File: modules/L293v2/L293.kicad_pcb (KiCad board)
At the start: 2 copper layers, 40.6 x 40.6 mm, 44 parts, among them J1 2, J10 11, J11 12, J12 13, J13 A0, J14 A1, J15 A2, J16 A3, J17 A4, J18 A5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

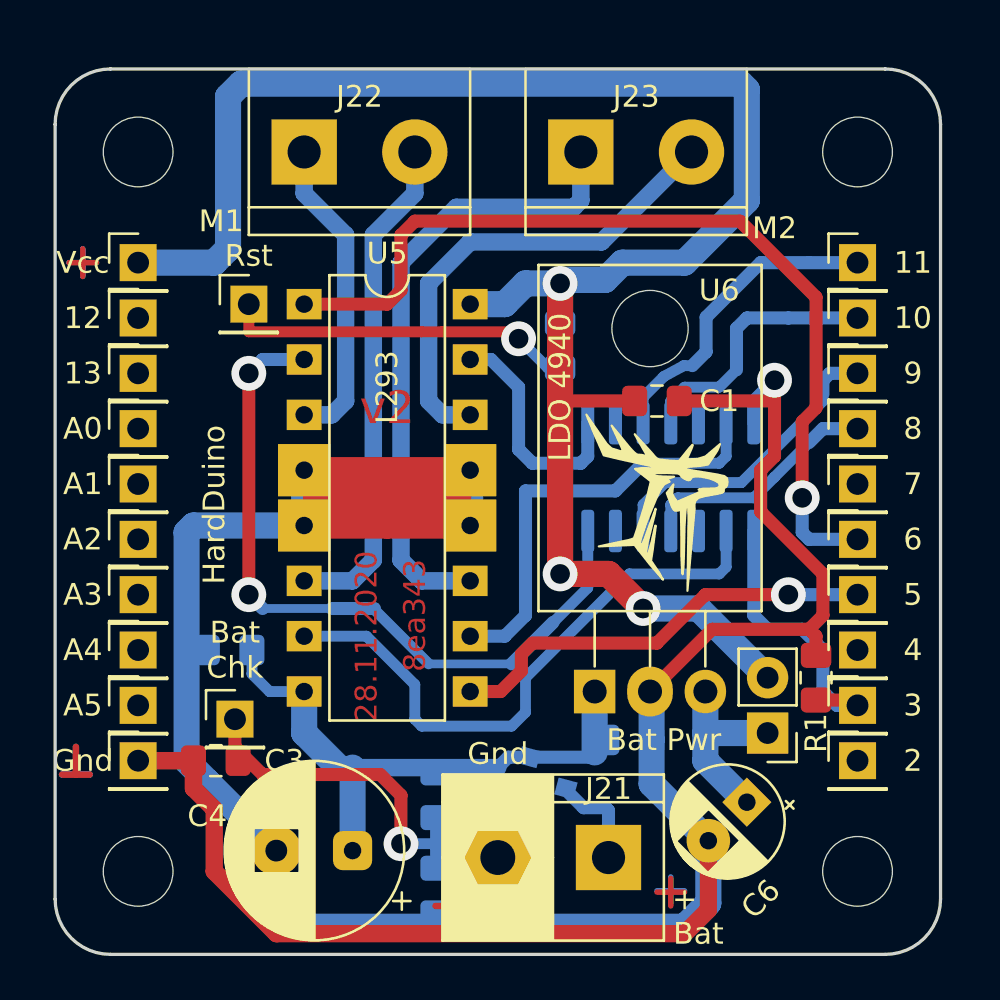
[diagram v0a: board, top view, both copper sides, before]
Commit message: 1x PCBs. Move holes to edges. Caution! This changes is uncompatible with previous versions...
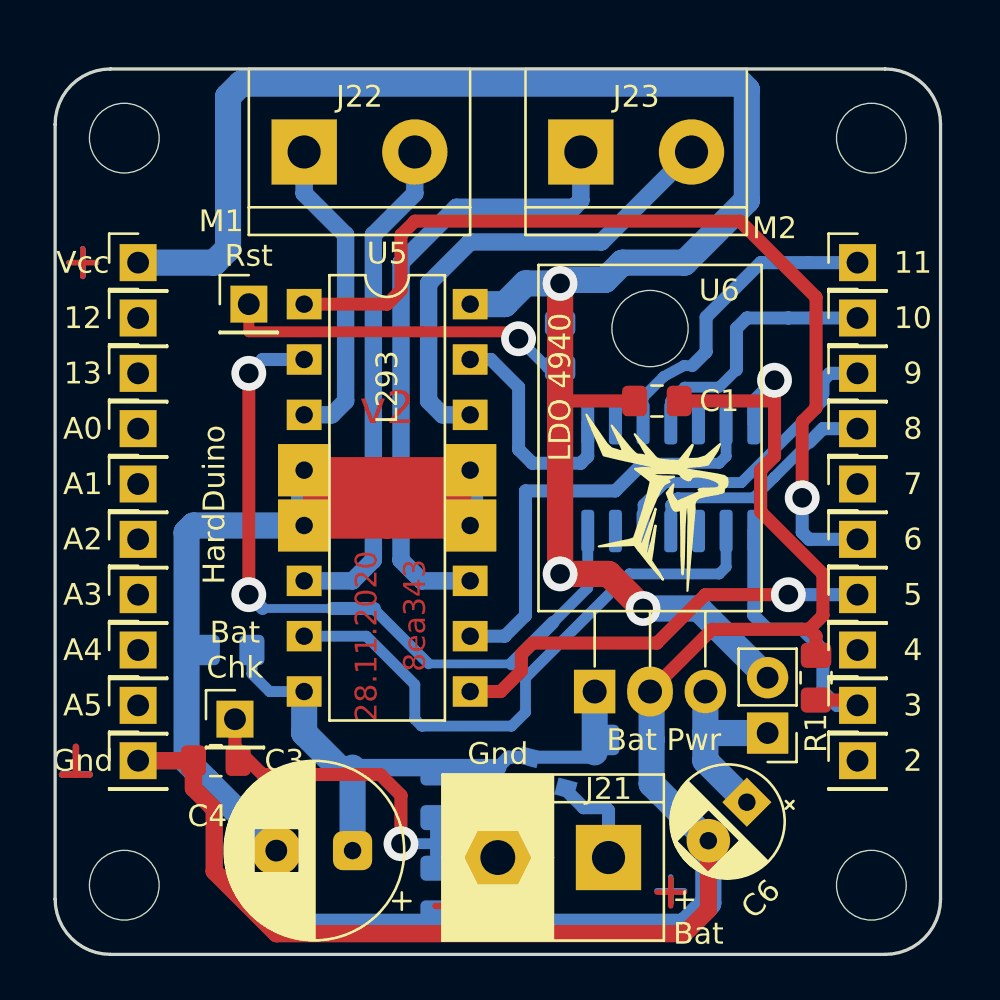
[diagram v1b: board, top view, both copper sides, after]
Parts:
- moved H2 0.90 mm to (92.1, 65.4)
- moved H4 0.90 mm to (126.4, 65.4)
- moved H1 0.90 mm to (92.1, 31.1)
- moved H3 0.90 mm to (126.4, 31.1)
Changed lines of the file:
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@@
   )
   (module MountingHole:MountingHole_3.2mm_M3 (layer F.Cu)
-    (at 92.71 31.75)
+    (at 92.0750 31.1150)
     (descr "Mounting Hole 3.2mm, no annular, M3")
     (tags "mounting hole 3.2mm no annular m3")
@@
   )
   (module MountingHole:MountingHole_3.2mm_M3 (layer F.Cu)
-    (at 92.71 64.77)
+    (at 92.0750 65.4050)
     (descr "Mounting Hole 3.2mm, no annular, M3")
     (tags "mounting hole 3.2mm no annular m3")
@@
   )
   (module MountingHole:MountingHole_3.2mm_M3 (layer F.Cu)
-    (at 125.73 31.75)
+    (at 126.3650 31.1150)
     (descr "Mounting Hole 3.2mm, no annular, M3")
     (tags "mounting hole 3.2mm no annular m3")
@@
   )
   (module MountingHole:MountingHole_3.2mm_M3 (layer F.Cu)
-    (at 125.73 64.77)
+    (at 126.3650 65.4050)
     (descr "Mounting Hole 3.2mm, no annular, M3")
     (tags "mounting hole 3.2mm no annular m3")

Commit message: Fix hash & version
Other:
- board text added: "21.02.2021"
- board text added: "b4d799"
- board text added: "v2.3"
- board text removed: "28.11.2020"
- board text removed: "8ea343"
- board text removed: "v2"

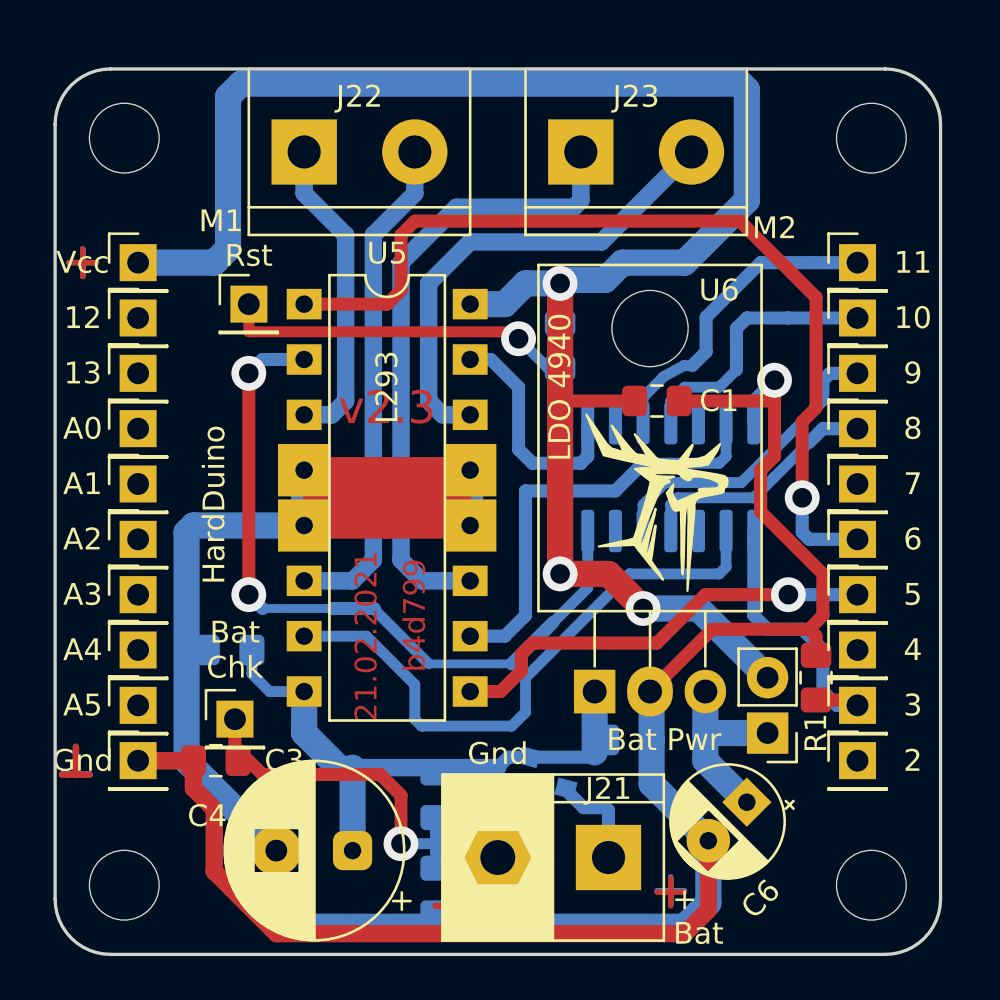
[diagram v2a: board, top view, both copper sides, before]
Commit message: All 1x shields was rotated clockwise
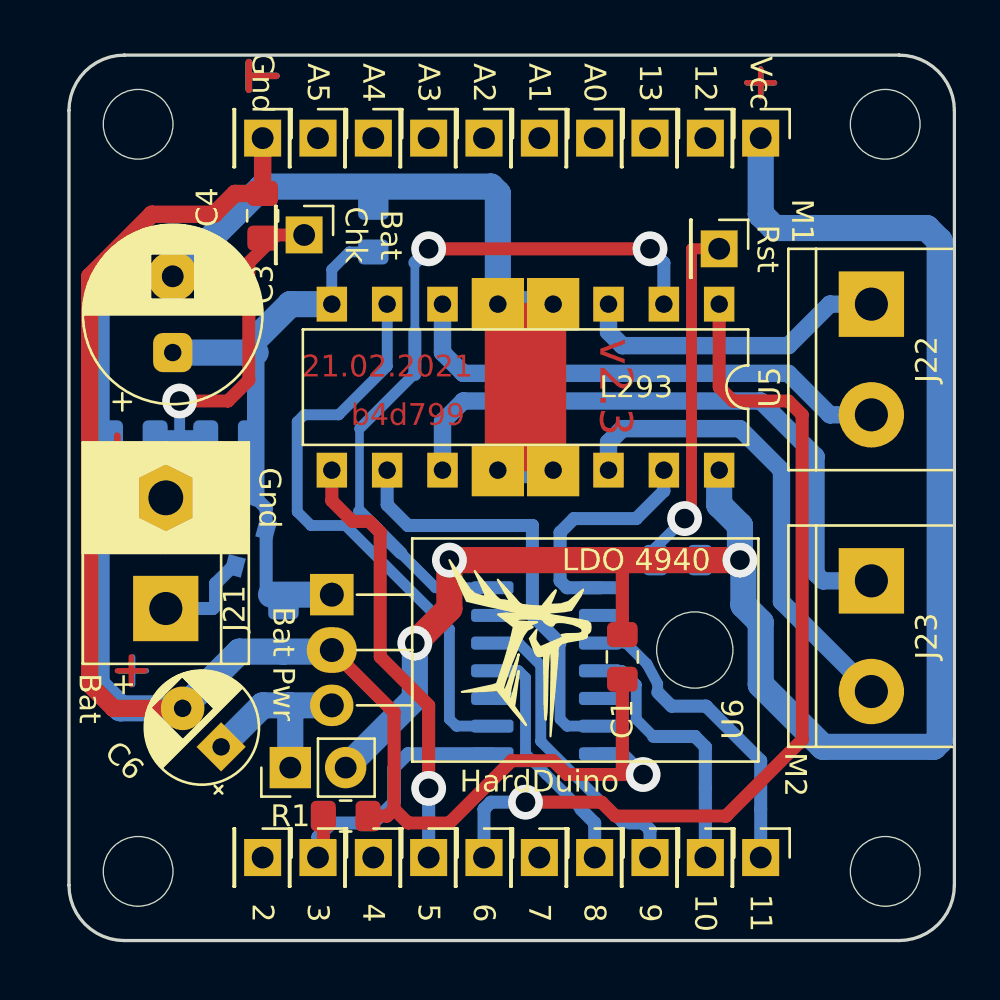
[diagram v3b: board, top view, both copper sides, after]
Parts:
- moved H1 34.9 mm to (127.0, 30.5), turned to 270 degrees
- moved H2 34.9 mm to (92.7, 30.5), turned to 270 degrees
- moved H3 33.7 mm to (127.0, 64.8), turned to 270 degrees
- moved H4 33.7 mm to (92.7, 64.8), turned to 270 degrees
- moved J19 29.1 mm to (121.3, 31.1), turned to 270 degrees
- moved J20 29.1 mm to (98.4, 31.1), turned to 270 degrees
- moved J1 27.7 mm to (98.4, 64.1), turned to 270 degrees
- moved J10 27.7 mm to (121.3, 64.1), turned to 270 degrees
- moved J11 27.3 mm to (118.7, 31.1), turned to 270 degrees
- moved J18 27.3 mm to (101.0, 31.1), turned to 270 degrees
- moved J22 27.0 mm to (126.4, 38.7), turned to 270 degrees
- moved J12 25.9 mm to (116.2, 31.1), turned to 270 degrees
- moved J17 25.9 mm to (103.5, 31.1), turned to 270 degrees
- moved J9 25.7 mm to (118.7, 64.1), turned to 270 degrees
- moved J2 25.7 mm to (101.0, 64.1), turned to 270 degrees
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
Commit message: Now all mounting holes have distance 31.92 x 31.1
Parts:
- moved H1 1.99 mm to (125.8, 32.1), turned to 0 degrees
- moved H2 1.99 mm to (93.9, 32.1), turned to 0 degrees
- moved H3 1.99 mm to (125.8, 63.2), turned to 0 degrees
- moved H4 1.99 mm to (93.9, 63.2), turned to 0 degrees
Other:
- board text added: "15.07.2021"
- board text added: "v2.5"
- board text removed: "21.02.2021"
- board text removed: "v2.3"
